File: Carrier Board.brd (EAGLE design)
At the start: 90 x 36.1 mm, 54 parts, among them J4 S2B-PH-SM4-TB(LF)(SN), J5 S2B-PH-SM4-TB(LF)(SN), Q1 MMBT2222A, SW2 MF-SW-TACT-6MM, U1 TMP36GRTZ, U2 TPL5010, U3 MB85RC256, U7 NAND

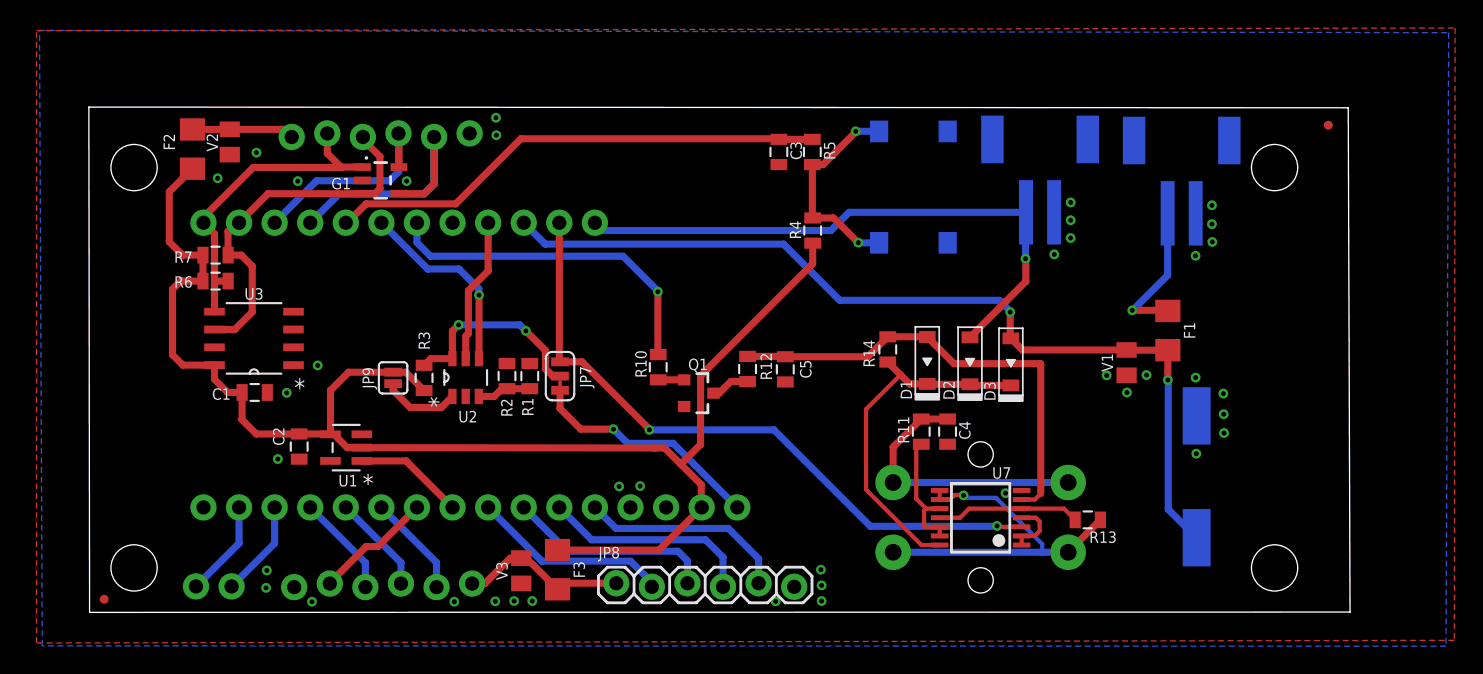
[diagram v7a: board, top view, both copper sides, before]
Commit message: Got ride of traces under components
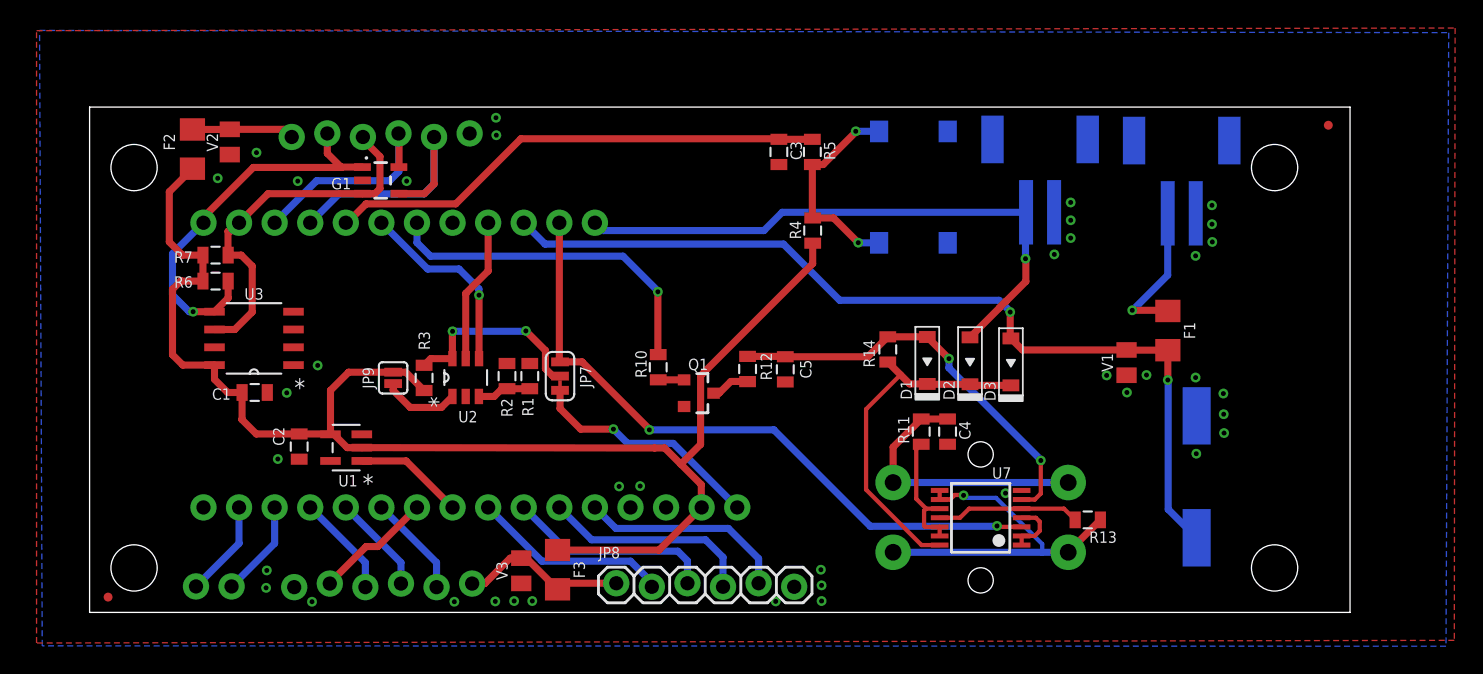
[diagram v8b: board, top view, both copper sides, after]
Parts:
- moved FD2 0.32 mm to (1.32, 1.09)
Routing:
- net SDA: track 23.7 -> 28.2 mm, vias 0 -> 1
- net !HARD-RESET: track 33.1 -> 29.5 mm, vias 0 -> 2
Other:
- outline, holes or cut-outs redrawn
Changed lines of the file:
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@@
 <board>
 <plain>
-<wire x1="0" y1="0" x2="89.9668" y2="0.0254" width="0" layer="20"/>
-<wire x1="89.9668" y1="0.0254" x2="89.8398" y2="36.0172" width="0" layer="20"/>
-<wire x1="89.8398" y1="36.0172" x2="-0.0508" y2="36.068" width="0" layer="20"/>
-<wire x1="-0.0508" y1="36.068" x2="0" y2="0" width="0" layer="20"/>
+<wire x1="0" y1="0" x2="89.9668" y2="0" width="0" layer="20"/>
+<wire x1="89.9668" y1="0" x2="89.9668" y2="36.068" width="0" layer="20"/>
+<wire x1="89.9668" y1="36.068" x2="0" y2="36.068" width="0" layer="20"/>
+<wire x1="0" y1="36.068" x2="0" y2="0" width="0" layer="20"/>
 <text x="10.8966" y="3.7084" size="0.8128" layer="26" font="vector" rot="MR0">Rx  Tx</text>
 <text x="59.9948" y="25.4254" size="0.8128" layer="26" font="vector" rot="MR0">+</text>
@@
 </element>
 <element name="FD1" library="SparkFun-Aesthetics" package="FIDUCIAL-MICRO" value="FIDUCIALUFIDUCIAL" x="88.4174" y="34.7726" smashed="yes"/>
-<element name="FD2" library="SparkFun-Aesthetics" package="FIDUCIAL-MICRO" value="FIDUCIALUFIDUCIAL" x="1.0414" y="0.9398" smashed="yes"/>
+<element name="FD2" library="SparkFun-Aesthetics" package="FIDUCIAL-MICRO" value="FIDUCIALUFIDUCIAL" x="1.3208" y="1.0922" smashed="yes"/>
 <element name="JP5" library="SparkFun" package="STAND-OFF" value="STAND-OFF" x="3.175" y="31.75" smashed="yes"/>
 <element name="JP3" library="SparkFun" package="STAND-OFF" value="STAND-OFF" x="84.582" y="31.75" smashed="yes"/>
@@
 <wire x1="11.6847375" y1="31.7602" x2="17.973" y2="31.7602" width="0.508" layer="1"/>
 <wire x1="8.128" y1="28.2034625" x2="11.6847375" y2="31.7602" width="0.508" layer="1"/>
-<wire x1="8.9154" y1="21.463" x2="8.9154" y2="23.622" width="0.508" layer="1"/>
-<wire x1="8.9154" y1="23.622" x2="8.9154" y2="27.0256" width="0.508" layer="1"/>
-<wire x1="8.9154" y1="27.0256" x2="8.128" y2="27.813" width="0.508" layer="1"/>
-<wire x1="9.8916" y1="23.6474" x2="8.9408" y2="23.6474" width="0.508" layer="1"/>
-<wire x1="8.9408" y1="23.6474" x2="8.9154" y2="23.622" width="0.508" layer="1"/>
+<wire x1="8.128" y1="27.813" x2="5.9182" y2="25.6032" width="0.508" layer="16"/>
+<wire x1="5.9182" y1="25.6032" x2="5.9182" y2="22.6568" width="0.508" layer="16"/>
+<wire x1="5.9182" y1="22.6568" x2="7.112" y2="21.463" width="0.508" layer="16"/>
+<via x="7.3914" y="21.463" extent="1-16" drill="0.35"/>
+<wire x1="7.3914" y1="21.463" x2="8.9154" y2="21.463" width="0.508" layer="1"/>
+<wire x1="7.112" y1="21.463" x2="7.3914" y2="21.463" width="0.508" layer="16"/>
+<wire x1="8.9154" y1="21.463" x2="9.8916" y2="22.4392" width="0.508" layer="1"/>
+<wire x1="9.8916" y1="22.4392" x2="9.8916" y2="23.6474" width="0.508" layer="1"/>
 </signal>
 <signal name="VCC">
@@
 <contactref element="J5" pad="2"/>
 <contactref element="D2" pad="ANODE"/>
-<wire x1="66.8434" y1="28.558" x2="54.212" y2="28.558" width="0.508" layer="16"/>
-<wire x1="54.212" y1="28.558" x2="52.9082" y2="27.2542" width="0.508" layer="16"/>
-<wire x1="52.9082" y1="27.2542" x2="36.6268" y2="27.2542" width="0.508" layer="16"/>
+<wire x1="66.8434" y1="28.558" x2="49.4368" y2="28.558" width="0.508" layer="16"/>
+<wire x1="49.4368" y1="28.558" x2="48.133" y2="27.2542" width="0.508" layer="16"/>
+<wire x1="48.133" y1="27.2542" x2="36.6268" y2="27.2542" width="0.508" layer="16"/>
 <wire x1="36.6268" y1="27.2542" x2="36.068" y2="27.813" width="0.508" layer="16"/>
 <wire x1="66.8274" y1="23.6206" x2="66.8274" y2="25.2222" width="0.508" layer="1"/>
@@
 <wire x1="26.3652" y1="24.511" x2="27.7876" y2="23.0886" width="0.508" layer="16"/>
 <wire x1="27.7876" y1="23.0886" x2="27.7876" y2="22.6354" width="0.508" layer="16"/>
-<wire x1="27.7876" y1="22.6314" x2="27.7876" y2="22.6354" width="0.508" layer="16"/>
 <wire x1="27.7876" y1="22.6354" x2="27.7978" y2="22.6456" width="0.508" layer="16"/>
 <via x="27.7978" y="22.6456" extent="1-16" drill="0.35"/>
@@
 <wire x1="56.9722" y1="19.6706" x2="59.7792" y2="19.6706" width="0.508" layer="1"/>
 <wire x1="59.7792" y1="19.6706" x2="59.7916" y2="19.6582" width="0.508" layer="1"/>
-<wire x1="59.7916" y1="19.6582" x2="61.6952" y2="17.7546" width="0.508" layer="1"/>
-<wire x1="61.6952" y1="17.7546" x2="67.8688" y2="17.7546" width="0.508" layer="1"/>
-<wire x1="67.8688" y1="17.7546" x2="67.8942" y2="17.7292" width="0.508" layer="1"/>
-<wire x1="67.8942" y1="17.7292" x2="67.8942" y2="8.4836" width="0.508" layer="1"/>
+<wire x1="61.3396" y1="18.1102" x2="59.7916" y2="19.6582" width="0.508" layer="1"/>
 <wire x1="67.8942" y1="8.4836" x2="67.467" y2="8.0564" width="0.3048" layer="1"/>
 <wire x1="67.467" y1="8.0564" x2="66.5266" y2="8.0564" width="0.3048" layer="1"/>
+<via x="61.3396" y="18.1102" extent="1-16" drill="0.35"/>
+<wire x1="61.3396" y1="18.1102" x2="61.3396" y2="17.4512" width="0.508" layer="16"/>
+<wire x1="61.3396" y1="17.4512" x2="67.8942" y2="10.8966" width="0.508" layer="16"/>
+<wire x1="67.8942" y1="10.8966" x2="67.8942" y2="10.8458" width="0.508" layer="16"/>
+<via x="67.8942" y="10.8458" extent="1-16" drill="0.35"/>
+<wire x1="67.8942" y1="10.8458" x2="67.8942" y2="8.4836" width="0.3048" layer="1"/>
 </signal>
 <signal name="N$1">
@@
 <contactref element="U2" pad="5"/>
 <contactref element="BORON" pad="D8"/>
-<wire x1="27.0386" y1="22.960075" x2="27.0386" y2="19.9012" width="0.508" layer="1"/>
-<wire x1="27.0386" y1="19.9012" x2="26.8478" y2="19.7104" width="0.508" layer="1"/>
+<wire x1="26.8478" y1="22.769275" x2="26.8478" y2="18.114" width="0.508" layer="1"/>
 <wire x1="28.448" y1="27.813" x2="28.448" y2="24.369475" width="0.508" layer="1"/>
-<wire x1="28.448" y1="24.369475" x2="27.0386" y2="22.960075" width="0.508" layer="1"/>
-<wire x1="26.8478" y1="19.7104" x2="26.8478" y2="18.114" width="0.508" layer="1"/>
+<wire x1="28.448" y1="24.369475" x2="26.8478" y2="22.769275" width="0.508" layer="1"/>
 </signal>
 <signal name="EN">
@@
 <wire x1="23.876" y1="17.6386" x2="24.3514" y2="18.114" width="0.508" layer="1"/>
 <wire x1="24.3514" y1="18.114" x2="25.8978" y2="18.114" width="0.508" layer="1"/>
-<wire x1="25.8978" y1="18.114" x2="25.9128" y2="18.099" width="0.508" layer="1"/>
 <wire x1="33.1818625" y1="16.8656" x2="33.5788" y2="16.8656" width="0.3048" layer="1"/>
-<wire x1="25.8978" y1="18.114" x2="25.8978" y2="20.0812" width="0.508" layer="1"/>
-<via x="26.3398" y="20.5232" extent="1-16" drill="0.35"/>
-<wire x1="30.7086" y1="20.5232" x2="31.1404" y2="20.0914" width="0.508" layer="16"/>
-<wire x1="30.7086" y1="20.5232" x2="26.3398" y2="20.5232" width="0.508" layer="16"/>
+<wire x1="25.8978" y1="18.114" x2="25.8978" y2="20.0558" width="0.508" layer="1"/>
+<via x="25.908" y="20.066" extent="1-16" drill="0.35"/>
+<wire x1="31.1404" y1="20.0914" x2="31.115" y2="20.066" width="0.508" layer="16"/>
+<wire x1="31.115" y1="20.066" x2="25.908" y2="20.066" width="0.508" layer="16"/>
 <via x="31.1404" y="20.0914" extent="1-16" drill="0.35"/>
 <wire x1="31.1404" y1="20.0914" x2="32.5374" y2="18.6944" width="0.508" layer="1"/>
@@
 <wire x1="33.0675625" y1="16.8656" x2="33.1818625" y2="16.8656" width="0.508" layer="1"/>
 <wire x1="32.5374" y1="17.3957625" x2="33.0675625" y2="16.8656" width="0.508" layer="1"/>
-<wire x1="25.8978" y1="20.0812" x2="26.3398" y2="20.5232" width="0.508" layer="1"/>
+<wire x1="25.8978" y1="20.0558" x2="25.908" y2="20.066" width="0.508" layer="1"/>
 </signal>
 <signal name="VDD">
